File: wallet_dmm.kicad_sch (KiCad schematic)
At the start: 20 parts, among them J1 Conn_01x04, Q1 T2N7002BK_LM, Q2 T2N7002BK_LM, SW1 REST_BUTTON, U1 TLC555xD, U2 STM32L051K8Tx, U3 MCP9700-E/TO

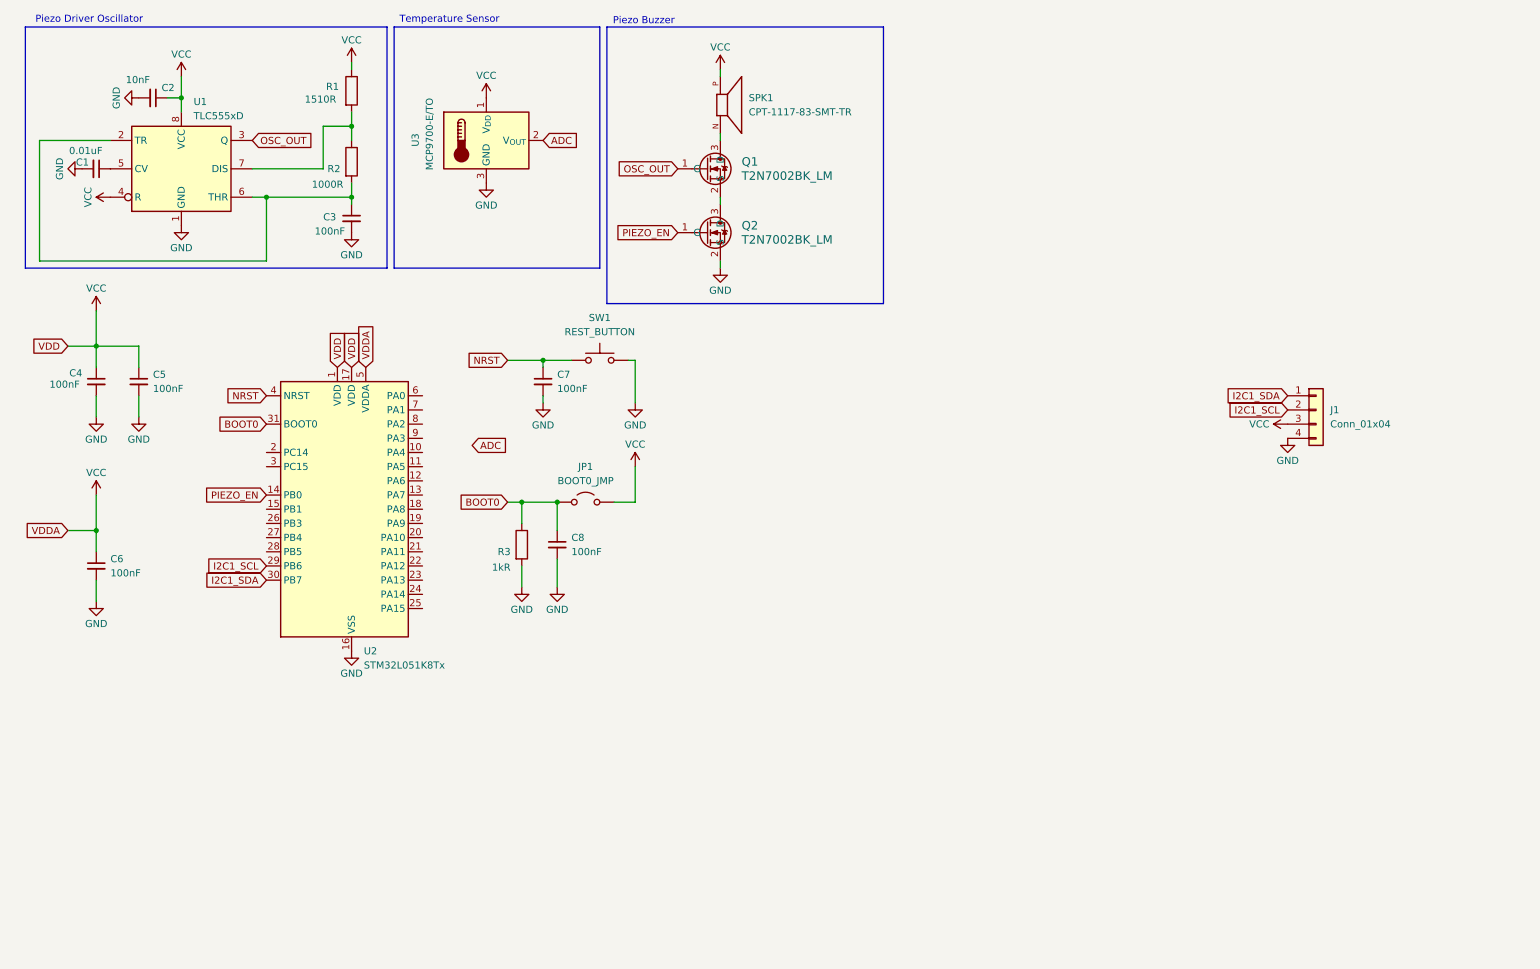
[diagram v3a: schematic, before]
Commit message: Completed PCB and some edits to schematic.
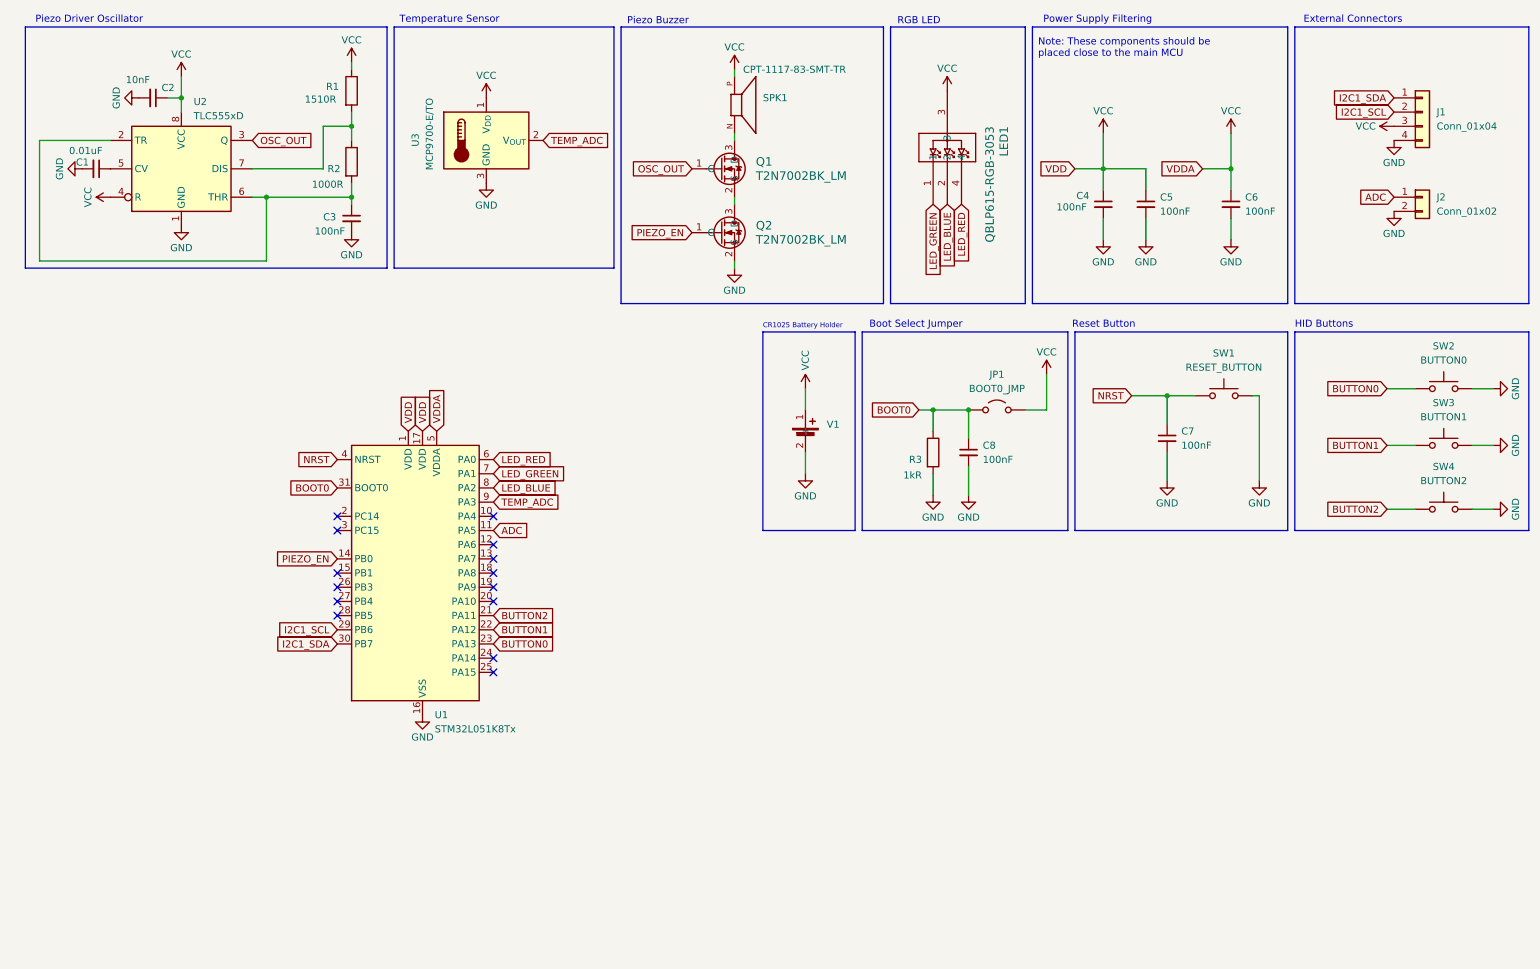
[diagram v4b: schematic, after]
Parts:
- added J2: Conn_01x02, project_specific_footprints:ADC_Connector, symbol Connector_Generic:Conn_01x02
- added LED1: QBLP615-RGB-3053, project_specific_footprints:QBLP615-RGB-3053_QTB, symbol QBLP615_RGB:QBLP615-RGB-3053
- added SW2: BUTTON0, project_specific_footprints:SW4_PTS815 SJM 250 SMTR LFS_CNK, symbol Switch:SW_MEC_5G
- added SW3: BUTTON1, project_specific_footprints:SW4_PTS815 SJM 250 SMTR LFS_CNK, symbol Switch:SW_MEC_5G
- added SW4: BUTTON2, project_specific_footprints:SW4_PTS815 SJM 250 SMTR LFS_CNK, symbol Switch:SW_MEC_5G
- added V1: ~, project_specific_footprints:BK-870_CR1025_Holder, symbol project_specific:BK-870_CR1025_Battery
- C1, C2, C3, C4, C5, C6, C7, C8: footprint (none) -> Capacitor_SMD:C_1206_3216Metric_Pad1.33x1.80mm_HandSolder
- J1: footprint project_specific:OLED_Header -> project_specific_footprints:OLED_Header
- Q1, Q2: footprint T2N7002BK:SOT23_TOS -> project_specific_footprints:T2N7002BK
- R1, R2, R3: footprint (none) -> Resistor_SMD:R_1206_3216Metric_Pad1.30x1.75mm_HandSolder
- SPK1: footprint wallet_dmm:XDCR_CPT-1117-83-SMT-TR -> project_specific_footprints:XDCR_CPT-1117-83-SMT-TR
- SW1: value REST_BUTTON -> RESET_BUTTON; footprint (none) -> project_specific_footprints:SW4_PTS815 SJM 250 SMTR LFS_CNK
- U3: footprint footprints:TO-92_MC_MCH -> Package_TO_SOT_THT:TO-92L_Inline
- renumbered U2 to U1, U1 to U2
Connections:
- net ADC: now also U1.11 (PA5), J2.1 (Pin_1); no longer U3.2 (V_{OUT})
- net GND: now also J2.2 (Pin_2), SW2.3 (B), SW2.4 (B), SW3.3 (B), SW3.4 (B), SW4.3 (B), SW4.4 (B), V1.2 (-)
- net VCC: now also LED1.3, V1.1 (+)
- net BUTTON2: now reaches U1.21 (PA11)
- net BUTTON2: now also SW4.1 (A), SW4.2 (A)
- net BUTTON1: now reaches U1.22 (PA12)
- net BUTTON1: now also SW3.1 (A), SW3.2 (A)
- net BUTTON0: now reaches U1.23 (PA13)
- net BUTTON0: now also SW2.1 (A), SW2.2 (A)
- net LED_RED: now reaches U1.6 (PA0)
- net LED_RED: now also LED1.4
- net LED_GREEN: now reaches U1.7 (PA1)
- net LED_GREEN: now also LED1.1
- net LED_BLUE: now reaches U1.8 (PA2)
- net LED_BLUE: now also LED1.2
- net TEMP_ADC: now reaches U1.9 (PA3)
- net TEMP_ADC: now also U3.2 (V_{OUT})
- no-connect marks 0 -> 14
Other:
- note added: "Boot Select Jumper"
- note added: "CR1025 Battery Holder"
- note added: "External Connectors"
- note added: "HID Buttons"
- note added: "Note: These components should be placed close to the main MCU"
- note added: "Power Supply Filtering"
- note added: "RGB LED"
- note added: "Reset Button"
- moved on the sheet: C4, C5, C6, C7, C8, J1, JP1, Q1, Q2, R3, SPK1, SW1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

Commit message: Revision 2
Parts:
- removed LED1: QBLP615-RGB-3053, project_specific_footprints:QBLP615-RGB-3053_QTB, symbol QBLP615_RGB:QBLP615-RGB-3053
- added C10, C11, C9: 100nF, Capacitor_SMD:C_0603_1608Metric_Pad1.08x0.95mm_HandSolder, symbol Device:C_Small
- added J3: Conn_01x04, Connector_PinHeader_2.54mm:PinHeader_1x04_P2.54mm_Vertical, symbol Connector_Generic:Conn_01x04
- added J4: Voltmeter, Connector_PinHeader_2.54mm:PinHeader_1x02_P2.54mm_Vertical, symbol Connector_Generic:Conn_01x02
- added LED1: QBLP615-RGB-3053, project:QBLP615-RGB-3053_QTB, symbol QBLP615_RGB_3053:QBLP615-RGB-3053
- added R10, R11: 1M, Resistor_SMD:R_0603_1608Metric_Pad0.98x0.95mm_HandSolder, symbol Device:R
- added R4: 10k, Resistor_SMD:R_0603_1608Metric_Pad0.98x0.95mm_HandSolder, symbol Device:R
- added R5: 100, Resistor_SMD:R_0603_1608Metric_Pad0.98x0.95mm_HandSolder, symbol Device:R
- added R6, R7, R8: 4.7k, Resistor_SMD:R_0603_1608Metric_Pad0.98x0.95mm_HandSolder, symbol Device:R
- added R9: 10M, Resistor_SMD:R_0603_1608Metric_Pad0.98x0.95mm_HandSolder, symbol Device:R
- C1, C2, C3, C4, C5, C6, C7, C8: footprint Capacitor_SMD:C_1206_3216Metric_Pad1.33x1.80mm_HandSolder -> Capacitor_SMD:C_0603_1608Metric_Pad1.08x0.95mm_HandSolder
- J1: footprint project_specific_footprints:OLED_Header -> custom:OLED_Header
- J2: value Conn_01x02 -> Voltmeter; footprint project_specific_footprints:ADC_Connector -> Connector_PinHeader_2.54mm:PinHeader_1x02_P2.54mm_Vertical
- Q1, Q2: footprint project_specific_footprints:T2N7002BK -> project:T2N7002BK
- R1, R2: footprint Resistor_SMD:R_1206_3216Metric_Pad1.30x1.75mm_HandSolder -> Resistor_SMD:R_0603_1608Metric_Pad0.98x0.95mm_HandSolder
- R3: value 1kR -> 10k; footprint Resistor_SMD:R_1206_3216Metric_Pad1.30x1.75mm_HandSolder -> Resistor_SMD:R_0603_1608Metric_Pad0.98x0.95mm_HandSolder
- SPK1: footprint project_specific_footprints:XDCR_CPT-1117-83-SMT-TR -> project:XDCR_CPT-1117-83-SMT-TR
- SW1, SW2, SW3, SW4: footprint project_specific_footprints:SW4_PTS815 SJM 250 SMTR LFS_CNK -> project:SW4_PTS815 SJM 250 SMTR LFS_CNK
- V1: footprint project_specific_footprints:BK-870_CR1025_Holder -> custom:BK-870-TR
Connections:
- net ADC: now also R10.1, R9.1; no longer J2.1 (Pin_1)
- net BUTTON0: now also C9.1, R6.2; no longer SW2.1 (A), SW2.2 (A)
- net BUTTON1: now also C10.1, R7.2; no longer SW3.1 (A), SW3.2 (A)
- net BUTTON2: now also C11.1, R8.2; no longer SW4.1 (A), SW4.2 (A)
- net GND: now also J2.1 (Pin_1), C10.2, C11.2, C9.2, J3.4 (Pin_4), J4.1 (Pin_1), R10.2; no longer J2.2 (Pin_2)
- net LED_BLUE: now also LED1.2
- net LED_GREEN: now also LED1.1
- net LED_RED: now also LED1.4
- net NRST: now also R4.2
- net VCC: now also J3.1 (Pin_1), LED1.3, R11.1, R4.1, R5.1
- net CONTINUITY: now reaches U1.10 (PA4)
- net CONTINUITY: now also J2.2 (Pin_2), J4.2 (Pin_2), R11.2, R9.2
- net SWCLK: now reaches U1.24 (PA14)
- net SWCLK: now also J3.3 (Pin_3)
- net SWDIO: now reaches U1.25 (PA15)
- net SWDIO: now also J3.2 (Pin_2)
- net at Q1.3 (D), SPK1.N: now also R5.2
- net OSC_OUT renamed PIEZO_OUT
- new net: R6.1, SW2.1 (A), SW2.2 (A)
- new net: R7.1, SW3.1 (A), SW3.2 (A)
- new net: R8.1, SW4.1 (A), SW4.2 (A)
- no-connect marks 14 -> 11
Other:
- note added: "Continuity Tester"
- note added: "Piezo Buzzer Driver"
- note added: "Voltmeter (10:1)"
- note removed: "Piezo Buzzer"
- company: (none) -> Nicholas Sara
- title: (none) -> Wallet DMM
- moved on the sheet: C7, C8, J1, J2, JP1, R3, SPK1, SW1, SW2, SW3, SW4, U1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
